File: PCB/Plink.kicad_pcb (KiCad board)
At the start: 2 copper layers, 30 x 30 mm, 34 parts, among them IC1 TLV75533PDBV, J1 USB_B_Mini, J2 STDC14, J3 Target STDC14, J4 I2C_OLED, U1 USBLC6-2SC6, U2 STM32F070CBTx, X1 NX3225GD, X2 Graphic

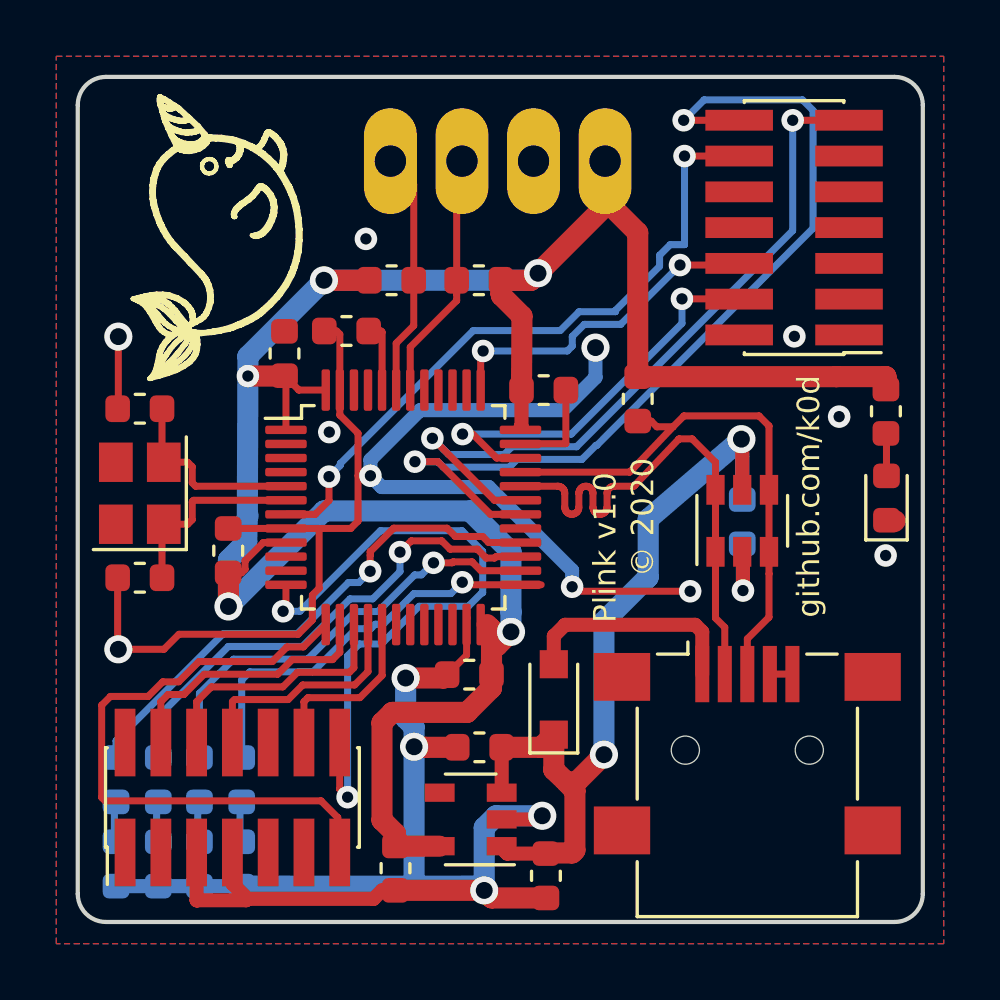
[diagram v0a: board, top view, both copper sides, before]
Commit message: Adds checklist, uart rx/tx solder bridges
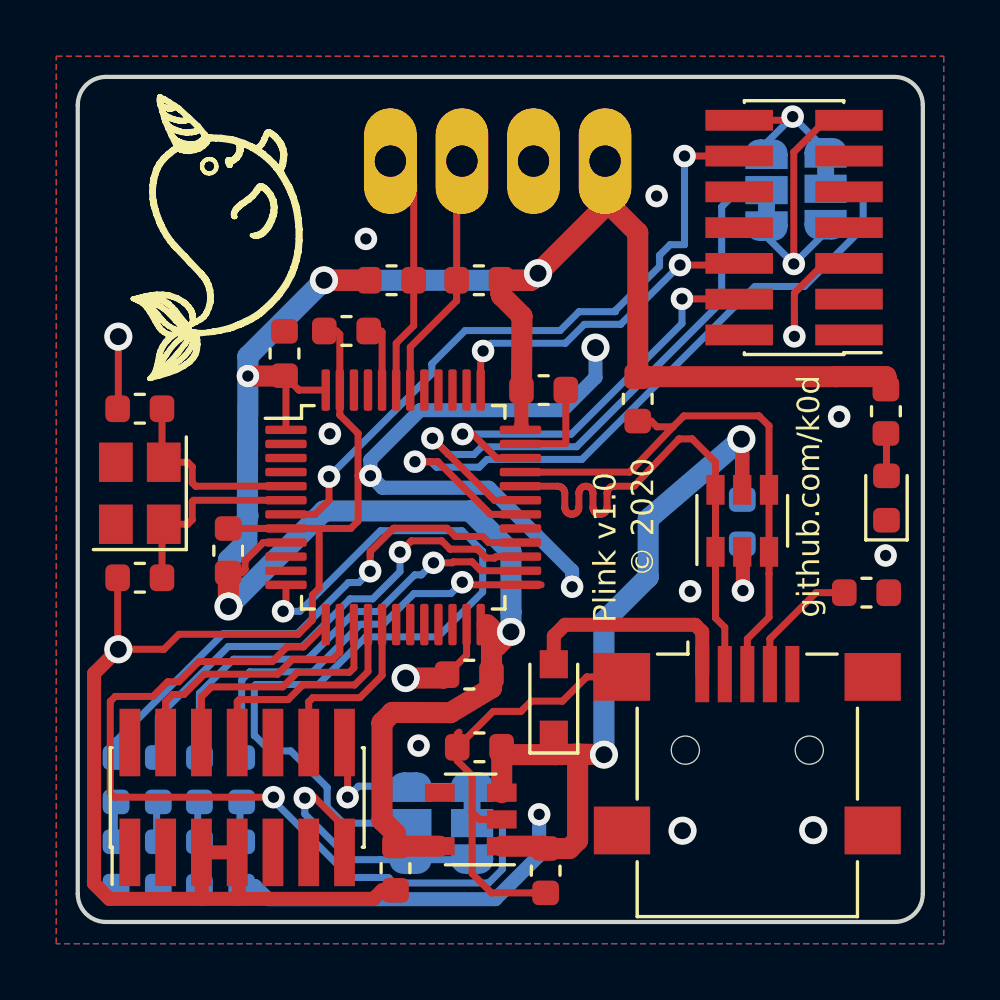
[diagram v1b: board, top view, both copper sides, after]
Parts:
- added JP1: SB_T_VCP_RX, Jumper:SolderJumper-3_P1.3mm_Bridged12_RoundedPad1.0x1.5mm, B.Cu at (40.0, 48.0)
- added JP2: SB_T_VCP_TX, Jumper:SolderJumper-3_P1.3mm_Bridged12_RoundedPad1.0x1.5mm, B.Cu at (42.2, 48.0)
- added JP3: SB_VCP_RX, Jumper:SolderJumper-3_P1.3mm_Bridged12_RoundedPad1.0x1.5mm, B.Cu at (52.6, 25.5)
- added JP4: SB_VCP_RX, Jumper:SolderJumper-3_P1.3mm_Bridged12_RoundedPad1.0x1.5mm, B.Cu at (54.8, 25.5)
- added R10: 100k, Resistor_SMD:R_0603_1608Metric, F.Cu at (56.2, 39.8)
- X2: value Graphic -> Narwahl
- moved C4 0.18 mm to (44.8, 49.7)
- moved J3 0.17 mm to (33.9, 47.1)
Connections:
- J1 pad 4: GND -> Net-(J1-Pad4)
- J2 pad 13: /VCP_RX -> /PIN_VCP_RX
- J2 pad 14: /VCP_TX -> /PIN_VCP_TX
- J3 pad 13: /T_VCP_RX -> /PIN_T_VCP_RX
- J3 pad 14: /T_VCP_TX -> /PIN_T_VCP_TX
- U2 pad 12: /T_VCP_TX -> /T_VCP_RX
- U2 pad 13: /T_VCP_RX -> /T_VCP_TX
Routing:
- net /PIN_T_VCP_RX: track 0.00 -> 11.8 mm, vias 0 -> 1
- net /PIN_VCP_RX: track 0.00 -> 10.8 mm, vias 0 -> 1
- net GND: track 108.5 -> 116.5 mm, vias 16 -> 18
- net /T_VCP_RX: track 22.4 -> 29.5 mm, vias 0 -> 1
- net /VCP_TX: track 33.5 -> 26.6 mm, vias 2 -> 1
- net /PIN_T_VCP_TX: track 0.00 -> 6.81 mm, vias 0 -> 1
- net /T_VCP_TX: track 24.1 -> 30.2 mm, vias 2 -> 1
- net /PIN_VCP_TX: track 0.00 -> 5.39 mm, vias 0 -> 1
- net Net-(J1-Pad4): track 0.00 -> 4.57 mm
- net /VCP_RX: track 26.3 -> 22.0 mm, vias 2 -> 1
- net +5V: track 29.9 -> 29.4 mm
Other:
- rule pad_to_mask_clearance: 0.2 -> 0.07

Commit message: v1.1
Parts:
- removed the C2 at (42.5, 45.3)
- removed the J4 at (56.7, 22.4)
- removed JP1: SB_T_VCP_RX, Jumper:SolderJumper-3_P1.3mm_Bridged12_RoundedPad1.0x1.5mm
- removed JP2: SB_T_VCP_TX, Jumper:SolderJumper-3_P1.3mm_Bridged12_RoundedPad1.0x1.5mm
- removed JP3, JP4: SB_VCP_RX, Jumper:SolderJumper-3_P1.3mm_Bridged12_RoundedPad1.0x1.5mm
- removed the R2 at (42.4, 28.7)
- removed the R5 at (56.9, 33.4)
- removed the U2 at (39.8, 36.8)
- added C3: 100nF, 01_Passives:C_0603, F.Cu at (45.0, 50.1)
- added C5: 1uF, 01_Passives:C_0603, F.Cu at (42.2, 50.2)
- added C6: 3.9pF, 01_Passives:C_0603, F.Cu at (32.1, 29.9)
- added C7: 3.9pF, 01_Passives:C_0603, F.Cu at (30.9, 30.7)
- added J3: STDC14, 01_Headers_1.27:M_2x07_1.27_V_SMD, F.Cu at (53.5, 26.8)
- added R11: 5k1, 01_Passives:R_0603, F.Cu at (56.2, 40.0)
- added R4: 4.7k, 01_Passives:R_0603, F.Cu at (41.5, 28.2)
- added R6: 330, 01_Passives:R_0603, F.Cu at (56.9, 33.5)
- added U1: W25Q128JVPIM TR, 01_Packages:WSON_8_6x5_1.27, B.Cu at (41.1, 47.0)
- added U3: STM32L433CCT6, 01_Packages:LQFP_48_7x7_0.5, F.Cu at (39.8, 36.8)
- added X3: 32.768KHz 12.5pF, 01_Packages:Crystal_2p_2012, F.Cu at (32.8, 32.1)
- C1: footprint Capacitor_SMD:C_0603_1608Metric -> 01_Passives:C_0603
- C10: renamed from C8; footprint Capacitor_SMD:C_0603_1608Metric -> 01_Passives:C_0603
- C11: renamed from C9; footprint Capacitor_SMD:C_0603_1608Metric -> 01_Passives:C_0603
- C12: renamed from C10; footprint Capacitor_SMD:C_0603_1608Metric -> 01_Passives:C_0603
- C13: renamed from C11; footprint Capacitor_SMD:C_0603_1608Metric -> 01_Passives:C_0603
- C2: renamed from C3; footprint Capacitor_SMD:C_0603_1608Metric -> 01_Passives:C_0603
- C4: value 1uF -> 100nF; footprint Capacitor_SMD:C_0603_1608Metric -> 01_Passives:C_0603; moved to B.Cu
- C8: renamed from C6; footprint Capacitor_SMD:C_0603_1608Metric -> 01_Passives:C_0603
- C9: renamed from C5; footprint Capacitor_SMD:C_0603_1608Metric -> 01_Passives:C_0603
- D1: footprint Diode_SMD:D_SOD-323_HandSoldering -> 01_Passives:D_SOD_323
- D2, D3, D4, D5, D6: footprint LED_SMD:LED_0603_1608Metric -> 01_Passives:LED_0603
- IC1: footprint Package_TO_SOT_SMD:SOT-23-5 -> 01_Packages:SOT-23-5
- J1: value USB_B_Mini -> USB_C_Socket_USB2.0; footprint Connector_USB:USB_Mini-B_Lumberg_2486_01_Horizontal -> 01_Connectors:USB_C_Socket-C319148
- J2: value STDC14 -> I2C_OLED; footprint Connector_PinHeader_1.27mm:PinHeader_2x07_P1.27mm_Vertical_SMD -> 00_Components:OLED_i2c; moved to B.Cu
- J4: renamed from J3; footprint Connector_PinHeader_1.27mm:PinHeader_2x07_P1.27mm_Vertical_SMD -> 01_Headers_1.27:M_2x07_1.27_V_SMD
- R1, R3: footprint Resistor_SMD:R_0603_1608Metric -> 01_Passives:R_0603
- R10: renamed from R9; footprint Resistor_SMD:R_0603_1608Metric -> 01_Passives:R_0603
- R2: renamed from R10; value 100k -> 5k1; footprint Resistor_SMD:R_0603_1608Metric -> 01_Passives:R_0603
- R5: renamed from R4; footprint Resistor_SMD:R_0603_1608Metric -> 01_Passives:R_0603
- R7: renamed from R6; footprint Resistor_SMD:R_0603_1608Metric -> 01_Passives:R_0603
- R8: renamed from R7; footprint Resistor_SMD:R_0603_1608Metric -> 01_Passives:R_0603
- R9: renamed from R8; footprint Resistor_SMD:R_0603_1608Metric -> 01_Passives:R_0603
- U2: renamed from U1; footprint Package_TO_SOT_SMD:SOT-23-6 -> 01_Packages:SOT-23-6
- X2: renamed from X1; value NX3225GD -> 8MHz 8pF; footprint Crystal:Crystal_SMD_3225-4Pin_3.2x2.5mm -> 01_Packages:Crystal_4p_3225
- moved C4 7.96 mm to (36.9, 49.7), turned to 0 degrees
- moved R2 7.75 mm to (48.5, 38.9), turned to 270 degrees
- moved D6 7.43 mm to (30.4, 42.0), turned to 0 degrees
- moved D5 6.07 mm to (30.4, 43.4), turned to 0 degrees
- moved J2 5.75 mm to (56.7, 22.0)
- moved R10 5.72 mm to (33.2, 42.0), turned to 180 degrees
- moved R3 5.33 mm to (44.6, 28.2), turned to 0 degrees
- moved D4 5.15 mm to (30.4, 44.8), turned to 0 degrees
- moved D3 4.94 mm to (30.4, 46.1), turned to 0 degrees
- moved R9 3.72 mm to (33.2, 43.4), turned to 180 degrees
- moved X1 2.47 mm to (33.5, 25.2), turned to 357 degrees
- moved C10 1.82 mm to (43.6, 41.7), turned to 90 degrees
- moved R8 1.82 mm to (33.2, 44.8), turned to 180 degrees
- moved C8 1.24 mm to (39.3, 48.4)
- moved J1 1.22 mm to (52.6, 46.4)
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- renumbered X2 to X1
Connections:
- C4 pad 2: +5V -> +3V3
- J2 pad 1: Net-(J2-Pad1) -> +3V3
- J2 pad 2: Net-(J2-Pad2) -> GND
- J2 pad 3: Net-(J2-Pad3) -> /I2C1_SCL
- J2 pad 4: /DBG_DIO -> /I2C1_SDA
- J4 pad 13: /PIN_T_VCP_RX -> /T_VCP_RX
- J4 pad 14: /PIN_T_VCP_TX -> /T_VCP_TX
- J4 pad 4: /T_DBG_DIO -> /T_SWDIO
- J4 pad 6: /T_DBG_CLK -> /T_SWCLK
- J4 pad 8: /T_DBG_SWO -> /T_SWO
- R2 pad 1: Net-(J1-Pad4) -> GND
- R2 pad 2: GND -> Net-(J1-PadA5)
- R3 pad 1: /I2C1_SDA -> /I2C1_SCL
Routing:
- net GND: track 116.5 -> 87.2 mm, vias 18 -> 14
- net /T_VCP_TX: track 30.2 -> 8.98 mm, vias 1 -> 2
- net /FLASH_D3: track 0.00 -> 20.8 mm, vias 0 -> 1
- net /DBG_DIO: track 14.7 -> 0.00 mm, vias 2 -> 0
- net /SWDIO: track 0.00 -> 14.6 mm, vias 0 -> 2
- net /FLASH_CLK: track 0.00 -> 14.4 mm, vias 0 -> 1
- net /SWO: track 0.00 -> 13.2 mm, vias 0 -> 2
- net /FLASH_D0: track 0.00 -> 12.3 mm, vias 0 -> 1
- net /DBG_CLK: track 11.8 -> 0.00 mm, vias 2 -> 0
- net /PIN_T_VCP_RX: track 11.8 -> 0.00 mm, vias 1 -> 0
- net /T_VCP_RX: track 29.5 -> 17.8 mm, vias 1 -> 2
- net /SWCLK: track 0.00 -> 11.5 mm, vias 0 -> 2
- net /FLASH_CS: track 0.00 -> 11.0 mm, vias 0 -> 1
- net /PIN_VCP_RX: track 10.8 -> 0.00 mm, vias 1 -> 0
- net /T_DBG_DIO: track 9.34 -> 0.00 mm
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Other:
- rule pad_to_mask_clearance: 0.07 -> 0
- board text added: "Plink v1.1"
- board text removed: "Plink v1.0"
